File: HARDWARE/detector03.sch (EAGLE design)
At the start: 33 parts, among them IC1 TL084P, IC2 7809T, IC3 7909

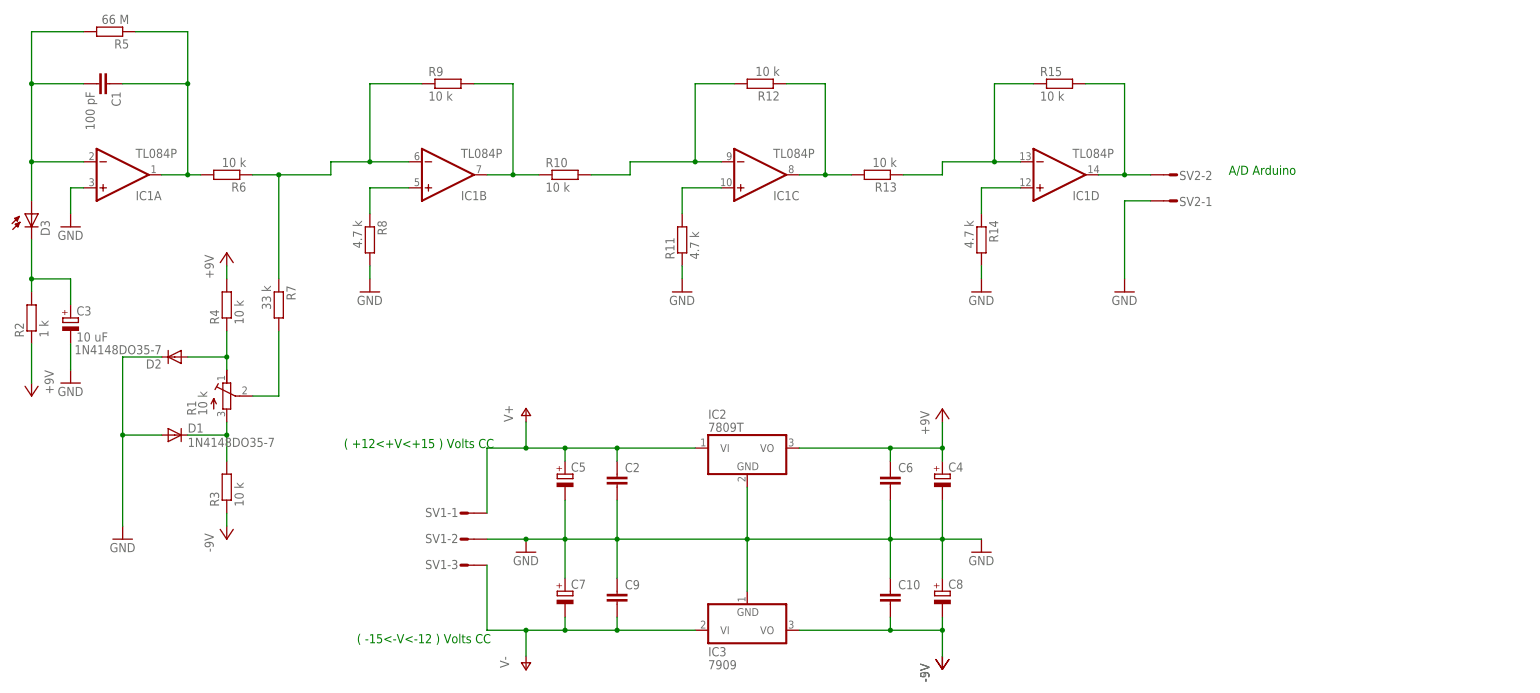
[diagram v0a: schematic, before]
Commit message: Adequações
-proteção ADC
-Correção detector00
-Adição detector05
-Inclusão de teste de tempo de leitura e de conjunto optoeletrônico
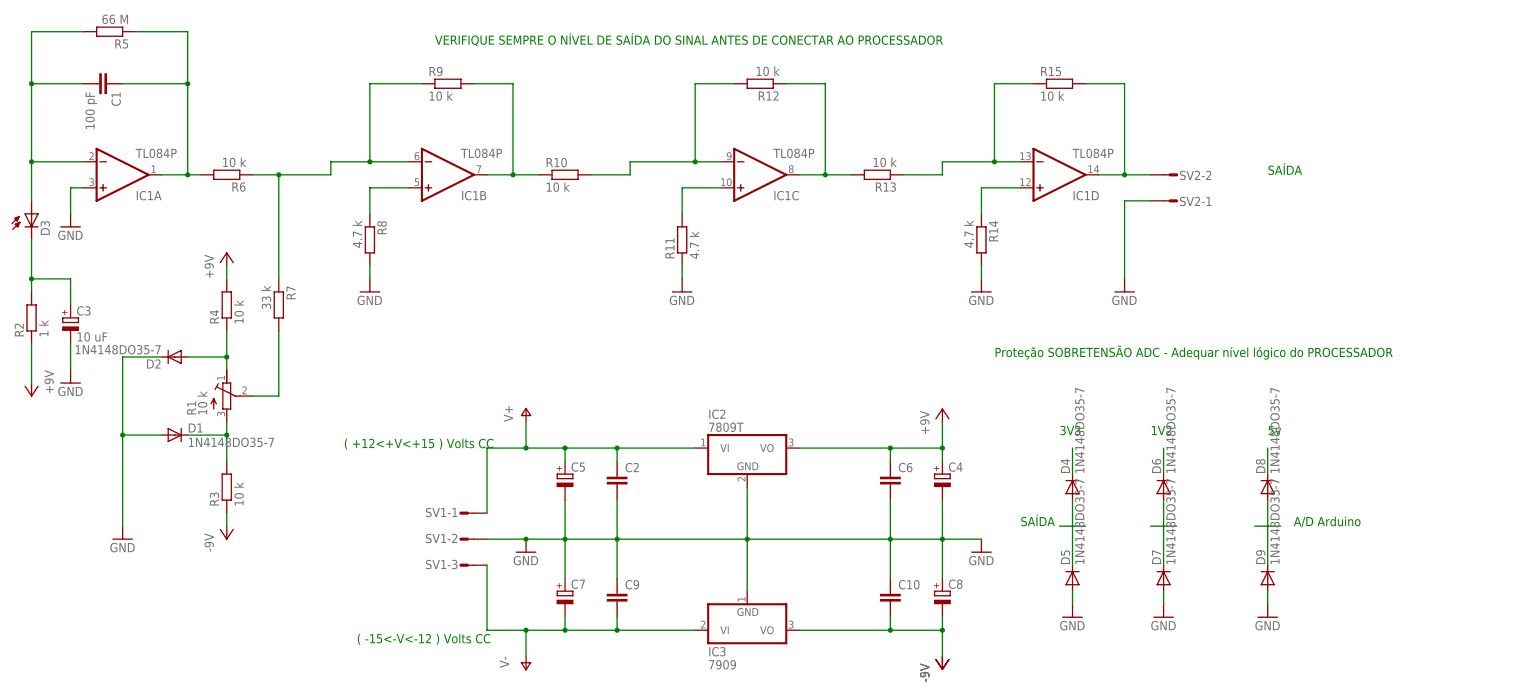
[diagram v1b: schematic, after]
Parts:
- added D4, D5, D6, D7, D8, D9: 1N4148DO35-7, diode:1N4148DO35-7
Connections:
- new net N$12: D4.C
- new net N$15: D4.A, D5.C
- new net N$16: D6.C
- new net N$19: D6.A, D7.C
- new net N$20: D8.C
- new net N$21: D8.A, D9.C
- net GND: now also D5.A, D7.A, D9.A
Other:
- note added: "1V2"
- note added: "3V3"
- note added: "5v"
- note added: "Proteção SOBRETENSÃO ADC - Adequar nível lógico do PROCESSADOR"
- note added: "SAÍDA"
- note added: "VERIFIQUE SEMPRE O NÍVEL DE SAÍDA DO SINAL ANTES DE CONECTAR AO PROCESSADOR"
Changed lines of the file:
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@@
 <part name="SV1" library="con-amp-mt" deviceset="L03P" device=""/>
 <part name="SV2" library="con-amp-mt" deviceset="L02P" device=""/>
+<part name="D4" library="diode" deviceset="1N4148" device="DO35-7"/>
+<part name="D5" library="diode" deviceset="1N4148" device="DO35-7"/>
+<part name="GND10" library="supply1" deviceset="GND" device=""/>
+<part name="D6" library="diode" deviceset="1N4148" device="DO35-7"/>
+<part name="D7" library="diode" deviceset="1N4148" device="DO35-7"/>
+<part name="GND11" library="supply1" deviceset="GND" device=""/>
+<part name="D8" library="diode" deviceset="1N4148" device="DO35-7"/>
+<part name="D9" library="diode" deviceset="1N4148" device="DO35-7"/>
+<part name="GND12" library="supply1" deviceset="GND" device=""/>
 </parts>
 <sheets>
 <sheet>
 <plain>
-<text x="220.98" y="68.58" size="1.778" layer="91">A/D Arduino</text>
 <text x="48.26" y="15.24" size="1.778" layer="91">( +12&lt;+V&lt;+15 ) Volts CC</text>
 <text x="50.8" y="-22.86" size="1.778" layer="91">( -15&lt;-V&lt;-12 ) Volts CC</text>
+<text x="187.96" y="17.78" size="1.778" layer="91">3V3</text>
+<text x="228.6" y="17.78" size="1.778" layer="91">5v</text>
+<text x="205.74" y="17.78" size="1.778" layer="91">1V2</text>
+<text x="233.68" y="0" size="1.778" layer="91">A/D Arduino</text>
+<text x="228.6" y="68.58" size="1.778" layer="91">SAÍDA</text>
+<text x="180.34" y="0" size="1.778" layer="91">SAÍDA</text>
+<text x="175.26" y="33.02" size="1.778" layer="91">Proteção SOBRETENSÃO ADC - Adequar nível lógico do PROCESSADOR</text>
+<text x="66.04" y="93.98" size="1.778" layer="91">VERIFIQUE SEMPRE O NÍVEL DE SAÍDA DO SINAL ANTES DE CONECTAR AO PROCESSADOR</text>
 </plain>
 <instances>
@@
 <instance part="SV2" gate="-1" x="210.82" y="63.5" rot="R180"/>
 <instance part="SV2" gate="-2" x="210.82" y="68.58" rot="R180"/>
+<instance part="D4" gate="G$1" x="190.5" y="7.62" rot="R90"/>
+<instance part="D5" gate="G$1" x="190.5" y="-10.16" rot="R90"/>
+<instance part="GND10" gate="1" x="190.5" y="-17.78"/>
+<instance part="D6" gate="G$1" x="208.28" y="7.62" rot="R90"/>
+<instance part="D7" gate="G$1" x="208.28" y="-10.16" rot="R90"/>
+<instance part="GND11" gate="1" x="208.28" y="-17.78"/>
+<instance part="D8" gate="G$1" x="228.6" y="7.62" rot="R90"/>
+<instance part="D9" gate="G$1" x="228.6" y="-10.16" rot="R90"/>
+<instance part="GND12" gate="1" x="228.6" y="-17.78"/>
 </instances>
 <busses>
@@
 <wire x1="200.66" y1="63.5" x2="200.66" y2="48.26" width="0.1524" layer="91"/>
 </segment>
+<segment>
+<pinref part="D5" gate="G$1" pin="A"/>
+<pinref part="GND10" gate="1" pin="GND"/>
+<wire x1="190.5" y1="-12.7" x2="190.5" y2="-15.24" width="0.1524" layer="91"/>
+</segment>
+<segment>
+<pinref part="D7" gate="G$1" pin="A"/>
+<pinref part="GND11" gate="1" pin="GND"/>
+<wire x1="208.28" y1="-12.7" x2="208.28" y2="-15.24" width="0.1524" layer="91"/>
+</segment>
+<segment>
+<pinref part="D9" gate="G$1" pin="A"/>
+<pinref part="GND12" gate="1" pin="GND"/>
+<wire x1="228.6" y1="-12.7" x2="228.6" y2="-15.24" width="0.1524" layer="91"/>
+</segment>
 </net>
 <net name="N$17" class="0">
@@
 </segment>
 </net>
+<net name="N$12" class="0">
+<segment>
+<pinref part="D4" gate="G$1" pin="C"/>
+<wire x1="190.5" y1="10.16" x2="190.5" y2="15.24" width="0.1524" layer="91"/>
+</segment>
+</net>
+<net name="N$15" class="0">
+<segment>
+<pinref part="D4" gate="G$1" pin="A"/>
+<pinref part="D5" gate="G$1" pin="C"/>
+<wire x1="190.5" y1="5.08" x2="190.5" y2="0" width="0.1524" layer="91"/>
+<wire x1="190.5" y1="0" x2="190.5" y2="-7.62" width="0.1524" layer="91"/>
+<wire x1="190.5" y1="0" x2="187.96" y2="0" width="0.1524" layer="91"/>
+<wire x1="190.5" y1="0" x2="193.04" y2="0" width="0.1524" layer="91"/>
+</segment>
+</net>
+<net name="N$16" class="0">
+<segment>
+<pinref part="D6" gate="G$1" pin="C"/>
+<wire x1="208.28" y1="10.16" x2="208.28" y2="15.24" width="0.1524" layer="91"/>
+</segment>
+</net>
+<net name="N$19" class="0">
+<segment>
+<pinref part="D6" gate="G$1" pin="A"/>
+<pinref part="D7" gate="G$1" pin="C"/>
+<wire x1="208.28" y1="5.08" x2="208.28" y2="0" width="0.1524" layer="91"/>
+<wire x1="208.28" y1="0" x2="208.28" y2="-7.62" width="0.1524" layer="91"/>
+<wire x1="208.28" y1="0" x2="205.74" y2="0" width="0.1524" layer="91"/>
+<wire x1="208.28" y1="0" x2="210.82" y2="0" width="0.1524" layer="91"/>
+</segment>
+</net>
+<net name="N$20" class="0">
+<segment>
+<pinref part="D8" gate="G$1" pin="C"/>
+<wire x1="228.6" y1="10.16" x2="228.6" y2="15.24" width="0.1524" layer="91"/>
+</segment>
+</net>
+<net name="N$21" class="0">
+<segment>
+<pinref part="D8" gate="G$1" pin="A"/>
+<pinref part="D9" gate="G$1" pin="C"/>
+<wire x1="228.6" y1="5.08" x2="228.6" y2="0" width="0.1524" layer="91"/>
+<wire x1="228.6" y1="0" x2="228.6" y2="-7.62" width="0.1524" layer="91"/>
+<wire x1="228.6" y1="0" x2="226.06" y2="0" width="0.1524" layer="91"/>
+<wire x1="228.6" y1="0" x2="231.14" y2="0" width="0.1524" layer="91"/>
+</segment>
+</net>
